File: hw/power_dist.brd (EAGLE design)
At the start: 80 x 50 mm, 99 parts, among them J1 JST-ZH6SMT_VERT, J2 JST-PH4SMT_VERT, J3 JST-PH5VERT, P1 XT30P, P2 XT30P, P3 XT30P, P4 XT30P, P5 XT30P, P6 XT30P, P7 XT90PW-M, Q1 PSMN4R8-100BSEJ, Q2 PSMN4R8-100BSEJ, Q3 PSMN4R8-100BSEJ, Q4 MF-DSC-SOT233-MMBT3904, Q5 MMBT5401 100V, U1 MAX15062AATA+T, U2 STM32G474CEU6, U3 TPS2490DGSR, U4 TCAN334G, U5 LT1787HVIMS8PBF, U6 STLM20DD9FUDFN-4L_STM-L

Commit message: Update the solder mask to be more amenable to oshstencil
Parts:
- U2: device precharge:QFN50P700X700X60-49N -> power_dist:QFN50P700X700X60-49N
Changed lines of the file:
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@@
 <layer number="29" name="tStop" color="7" fill="3" visible="no" active="yes"/>
 <layer number="30" name="bStop" color="7" fill="6" visible="no" active="yes"/>
-<layer number="31" name="tCream" color="7" fill="4" visible="no" active="yes"/>
+<layer number="31" name="tCream" color="7" fill="4" visible="yes" active="yes"/>
 <layer number="32" name="bCream" color="7" fill="5" visible="no" active="yes"/>
 <layer number="33" name="tFinish" color="6" fill="3" visible="no" active="yes"/>
@@
 <attribute name="POPULATE" value="1" x="76" y="13" size="1.778" layer="27" rot="R90" display="off"/>
 </element>
-<element name="U2" library="precharge" package="QFN50P700X700X60-49N" value="STM32G474CEU6" x="35.4" y="13.2" smashed="yes" rot="R180">
+<element name="U2" library="power_dist" package="QFN50P700X700X60-49N" value="STM32G474CEU6" x="35.4" y="13.2" smashed="yes" rot="R180">
 <attribute name="DESCRIPTION" value="STMICROELECTRONICS - STM32G474CEU6 - MCU, 32BIT, 170MHZ, UFQFPN-48" x="35.4" y="13.2" size="1.778" layer="27" rot="R180" display="off"/>
 <attribute name="HEIGHT" value="0.6mm" x="35.4" y="13.2" size="1.778" layer="27" rot="R180" display="off"/>

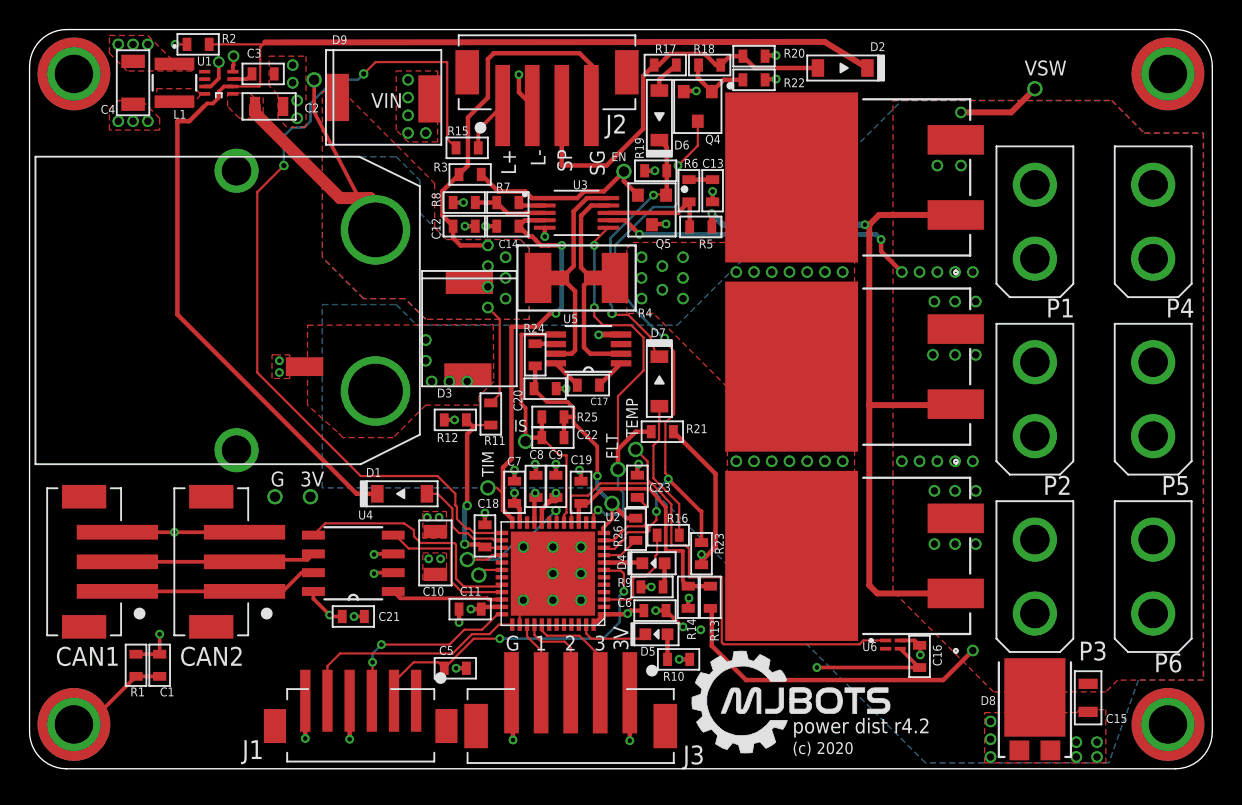
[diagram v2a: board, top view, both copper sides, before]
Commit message: Start on r4.3
This version dispenses with all the latching junk for main power, just
leaving it for the 3.3V rail.  Now, the stm32 is completely
responsible for turning the main power on and off, which could allow
it to reset the hot swap controller if need be.
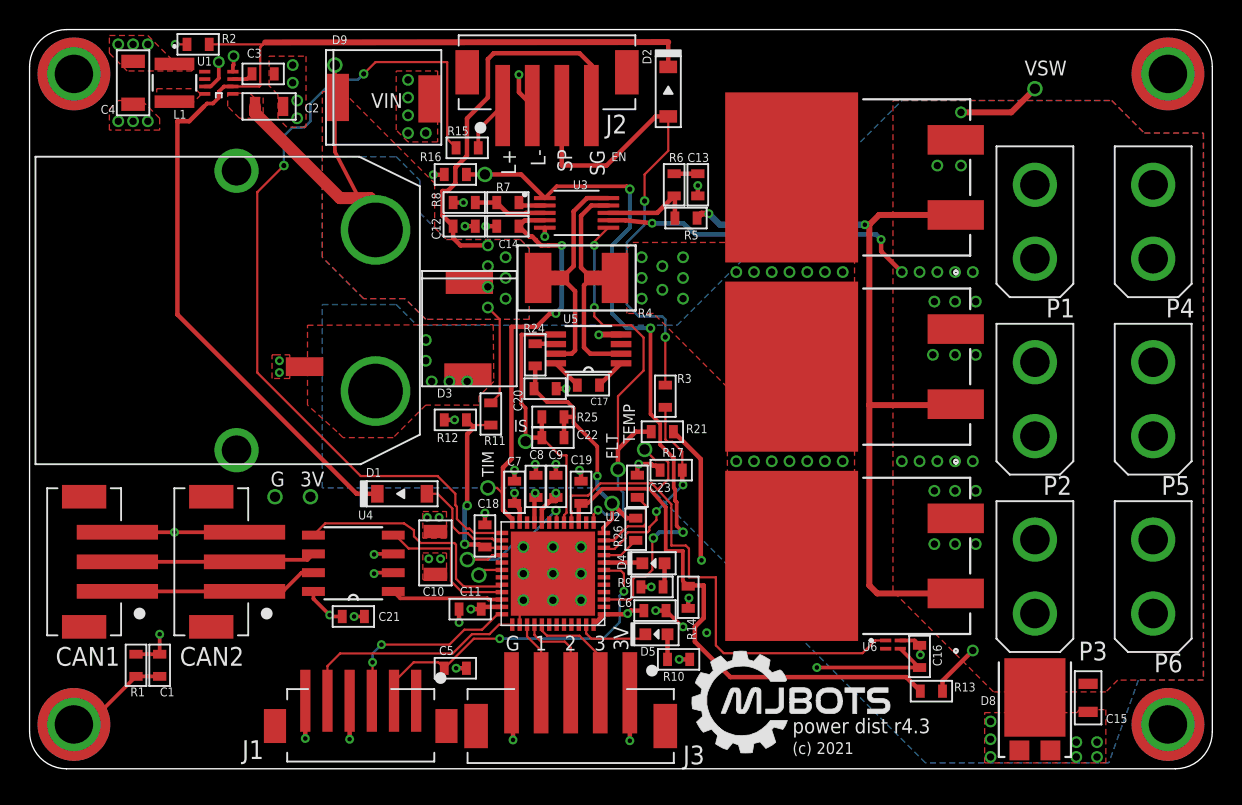
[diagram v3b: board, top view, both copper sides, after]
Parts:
- removed D6, D7: MF-DIO-SOD123-1N4148, mfdiscretesemi:SOD-123
- removed Q4: MF-DSC-SOT233-MMBT3904, mfdiscretesemi:SOT-23-3
- removed Q5: MMBT5401 100V, mfdiscretesemi:SOT-23-3
- removed R18: 2M, mfpassives:R0603
- removed R19: 200k, mfpassives:R0603
- removed R20: 100k, mfpassives:R0603
- removed R22: DNP, mfpassives:R0603
- removed R23: 33k, mfpassives:R0603
- R16: value 1k -> 200k 1%
- R17: value 500k -> 200k 1%
- R3: value 2M -> 200k 1%
- moved R16 28.3 mm to (28.8, 40.2), turned to 0 degrees
- moved R17 27.4 mm to (43.4, 20.2)
- moved R3 20.0 mm to (43.0, 25.2), turned to 90 degrees
- moved R13 16.2 mm to (61.0, 5.25), turned to 0 degrees
- moved D2 11.9 mm to (43.2, 45.8), turned to 270 degrees
- moved DB_LEN 9.40 mm to (30.8, 40.2)
- moved DB_VIN 1.72 mm to (20.6, 47.6)
- moved R5 1.17 mm to (44.4, 37.2)
- moved C13 1.08 mm to (45.2, 39.5)
- moved R6 1.08 mm to (43.6, 39.5)
- moved DB_TEMP 0.60 mm to (41.6, 21.6)
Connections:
- removed net LTC_EN: DB_LEN.P$1, Q5.P$2, R3.P$1, U3.1
- removed net N$11: Q4.P$1, R18.P$1, R22.P$2
- removed net N$13: D6.CATHODE, D7.CATHODE, Q5.P$1, R19.P$2
- removed net N$17: D6.ANODE, R17.P$1
- removed net N$18: D7.ANODE, R16.P$1
- removed net PWR_OVERRIDE: R16.P$2, U2.3
- new net TPS_EN: DB_LEN.P$1, R16.P$2, U2.3, U3.1
- net +24V: no longer R3.P$2
- net GND: now also R16.P$1, R17.P$2; no longer Q4.P$2, Q5.P$3, R19.P$1, R20.P$1, R22.P$1
- net PWR_SW: now also R3.P$2; no longer R17.P$2, R18.P$2, R20.P$2
- net SNS_PWR_SW: now also R17.P$1, R3.P$1; no longer Q4.P$3, R23.P$1
- net VCC: no longer R23.P$2
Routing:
- net TPS_EN: track 0.00 -> 47.9 mm, vias 0 -> 4
- net SNS_PWR_SW: track 42.3 -> 13.7 mm, vias 4 -> 2
- net VSWITCHED_SAMP: track 16.2 -> 36.5 mm
- net N$13: track 19.0 -> 0.00 mm, vias 2 -> 0
- net VSWITCHED: track 49.4 -> 30.9 mm
- net LTC_EN: track 13.1 -> 0.00 mm
- net 3V3_EN: track 86.4 -> 74.1 mm
- net N$18: track 9.62 -> 0.00 mm
- net PWR_OVERRIDE: track 7.30 -> 0.00 mm
- net PWR_SW: track 27.5 -> 34.0 mm, vias 0 -> 2
- net N$11: track 4.63 -> 0.00 mm
- net VCC: track 52.1 -> 49.8 mm
- net N$17: track 2.27 -> 0.00 mm
- net FET_TEMP: track 36.2 -> 38.2 mm
- net GND: track 67.6 -> 65.9 mm, vias 53 -> 50
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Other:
- board text added: "(c) 2021"
- board text added: "power dist r4.3"
- board text removed: "(c) 2020"
- board text removed: "power dist r4.2"

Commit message: Switch the LTC1787 filter to a 0.1uF
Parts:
- C17: value DNP -> 0.1uF
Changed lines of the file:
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@@
 <attribute name="PURCHASE-URL" value="https://pricing.snapeda.com/search/part/LT1787HVIMS8#PBF/?ref=eda" x="37.8" y="28.4" size="1.778" layer="27" rot="R180" display="off"/>
 </element>
-<element name="C17" library="mfpassives" package="C0603" value="DNP" x="37.8" y="25.95" smashed="yes" rot="R180">
+<element name="C17" library="mfpassives" package="C0603" value="0.1uF" x="37.8" y="25.95" smashed="yes" rot="R180">
 <attribute name="DIELECTRIC" value="" x="37.8" y="25.95" size="1.778" layer="27" rot="R180" display="off"/>
-<attribute name="HOUSEPART" value="" x="37.8" y="25.95" size="1.778" layer="27" rot="R180" display="off"/>
-<attribute name="MPN" value="" x="37.8" y="25.95" size="1.778" layer="27" rot="R180" display="off"/>
+<attribute name="HOUSEPART" value="1" x="37.8" y="25.95" size="1.778" layer="27" rot="R180" display="off"/>
+<attribute name="MPN" value="MF-CAP-0603-0.1uF" x="37.8" y="25.95" size="1.778" layer="27" rot="R180" display="off"/>
 <attribute name="NAME" x="39.15" y="25.1" size="0.5" layer="25" font="vector" ratio="10" rot="R180"/>
-<attribute name="POPULATE" value="0" x="37.8" y="25.95" size="1.778" layer="27" rot="R180" display="off"/>
+<attribute name="POPULATE" value="1" x="37.8" y="25.95" size="1.778" layer="27" rot="R180" display="off"/>
 <attribute name="TOLERANCE" value="" x="37.8" y="25.95" size="1.778" layer="27" rot="R180" display="off"/>
 <attribute name="URL" value="" x="37.8" y="25.95" size="1.778" layer="27" rot="R180" display="off"/>

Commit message: Updates for r4.3
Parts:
- added D6: 3V ZENER, mfdiscretesemi:SOD-123
- added Q4, Q5: (no value), mfdiscretesemi:SOT-23-3
- added R18: 100k 1%, mfpassives:R0603
- added R19: 499k 1%, mfpassives:R0603
- added R20: 47k 1%, mfpassives:R0603
- added R22: 200k 1%, mfpassives:R0603
- R16: value 200k 1% -> 100k
- moved R17 30.3 mm to (53.4, 48.8), turned to 0 degrees
- moved R3 24.7 mm to (50.4, 48.8), turned to 180 degrees
- moved R16 15.5 mm to (44.3, 41.9), turned to 180 degrees
- moved DB_LEN 11.1 mm to (41.8, 38.9)
- moved D2 3.23 mm to (44.4, 48.8), turned to 0 degrees
- moved R15 1.61 mm to (28.2, 41.2)
- moved J2 0.57 mm to (34.6, 47.0)
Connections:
- new net N$11: Q5.P$3, R19.P$2
- new net N$12: R18.P$2, R19.P$1, U3.1
- new net N$13: Q4.P$3, R22.P$1
- new net N$16: Q5.P$1, R20.P$1, R22.P$2
- net +24V: now also Q5.P$2, R20.P$2
- net GND: now also D6.ANODE, Q4.P$2, R18.P$1
- net SNS_PWR_SW: now also D6.CATHODE
- net TPS_EN: now also Q4.P$1; no longer U3.1
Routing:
- net SNS_PWR_SW: track 13.7 -> 52.9 mm, vias 2 -> 4
- net PWR_SW: track 34.0 -> 20.1 mm
- net N$16: track 0.00 -> 6.61 mm
- net +24V: track 58.3 -> 63.9 mm
- net TPS_EN: track 47.9 -> 42.6 mm
- net GND: track 65.9 -> 69.8 mm, vias 50 -> 53
- net PWR_LED: track 58.6 -> 54.9 mm
- net N$11: track 0.00 -> 3.46 mm
- net N$13: track 0.00 -> 3.44 mm
- net N$12: track 0.00 -> 3.02 mm
- net 3V3_EN: track 74.1 -> 72.3 mm
- net N$2: track 3.54 -> 4.36 mm
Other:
- board text added: "W"
- board text removed: "SG"
- board text removed: "SP"

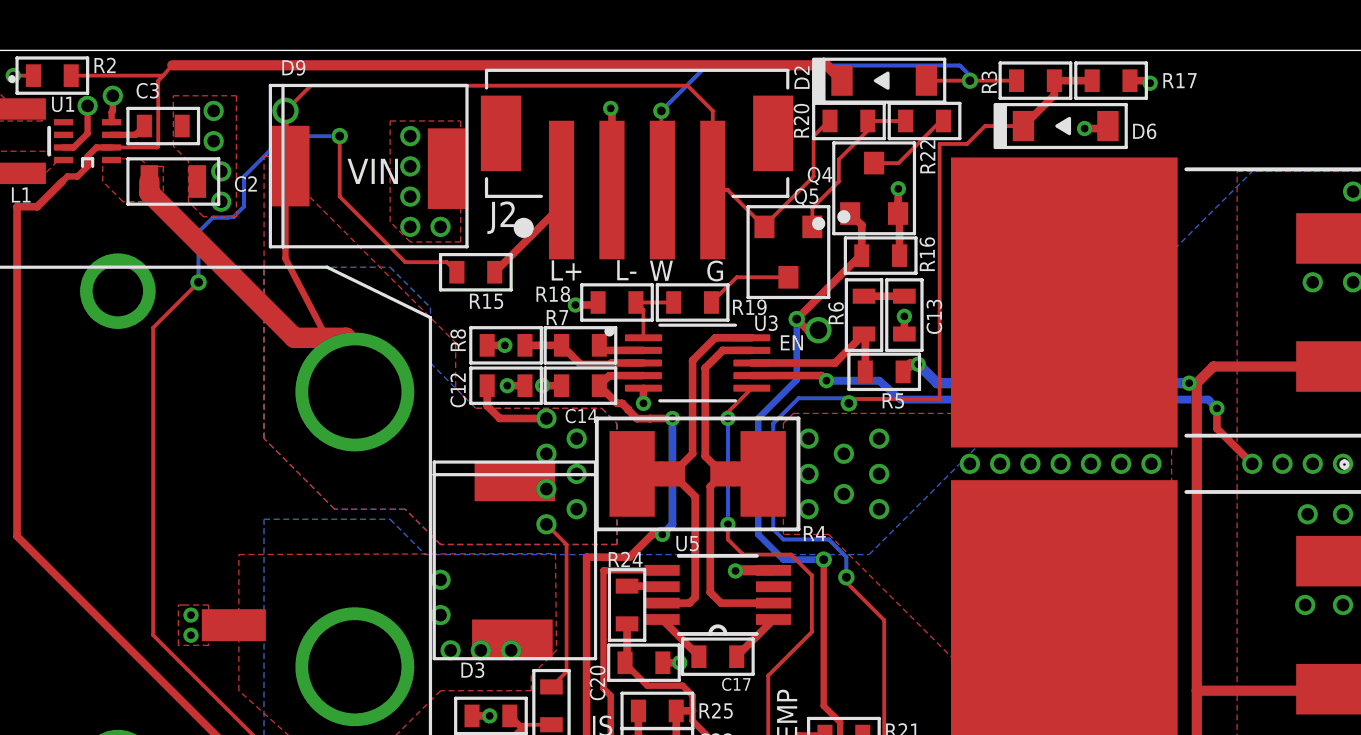
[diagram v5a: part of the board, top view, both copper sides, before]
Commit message: Move some wires further apart
Reduce the paste fill ratio under the stm32
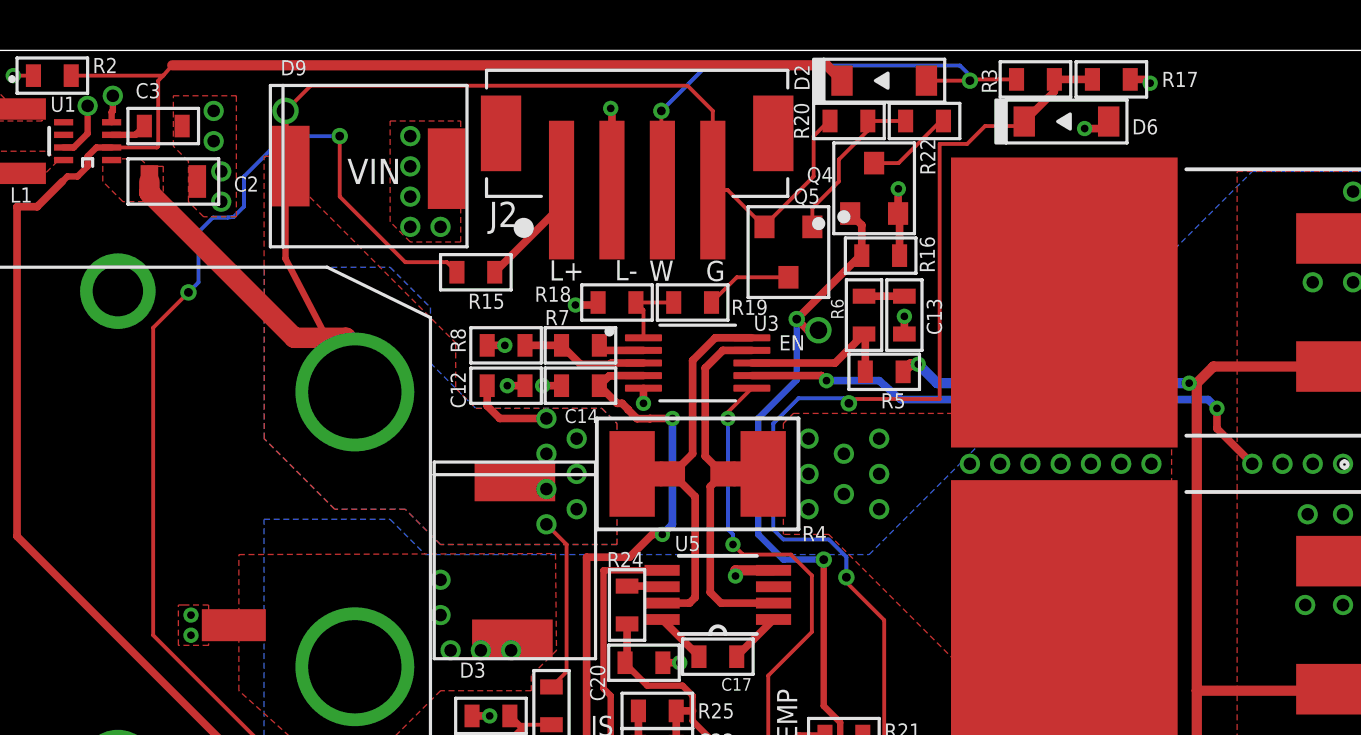
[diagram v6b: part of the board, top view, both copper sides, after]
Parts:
- moved D6 0.18 mm to (51.6, 47.2)
- moved R17 0.05 mm to (53.4, 48.9)
- moved R3 0.05 mm to (50.4, 48.9)
